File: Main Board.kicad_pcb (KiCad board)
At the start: 4 copper layers, 161 x 92 mm, 369 parts, among them J1 Motor Y, J10 CA58SUB-B, J11 PC6 EPSON MAINBOARD, J12 Y AXIS, J13 Z AXIS, J14 LED 1, J15 LED 2, J16 Power Input, J17 VS, J18 12V, J19 5V, J2 Motor Z, J20 3.3V, J21 TABLE SENSOR, J22 INPUT1, J23 INPUT2, J24 PHOTO SENSOR EMITER, J25 PHOTO SENSOR RECEIVER, J26 ANALOG, J27 INPUT3, J28 OUT1, J29 OUT2, J3 USB_B, J30 RELAY, J31 EMERGENCY, J32 EPSON POWER IN, J33 EPSON BOARD POWER, J34 Display, J35 SPI Interface, J36 I2C Interface, J37 LED4, J38 LED3, J39 Key 3, J4 SWD, J40 Key 4, J41 Key 1, J42 Key 2, J5 DEBUG, J6 LIMIT Y BACK, J7 LIMIT Y FRONT, J8 LIMIT Z UP, J9 LIMIT Z DOWN, K1 S13-24V-2C, Q1 2N7002K, Q10 2N7002K, Q11 BC817, Q12 BC817, Q13 BC817, Q14 2N7002K, Q15 2N7002K, Q16 2N7002K, Q17 BC817, Q18 2N7002K, Q19 2N7002K, Q2 2N7002K, Q20 2N7002K, Q21 2N7002K, Q3 2N7002K, Q4 2N7002K, Q5 2N7002K, Q6 2N7002K, Q7 2N7002K, Q8 YJS9435A, Q9 2N7002K, U1 TMC2209-LA, U10 74HC2G32, U11 74HC245, U12 SHTC3, U2 TMC2209-LA, U3 STM32F401VETx, U4 USBUF02W6, U5 74HC245, U6 MCP16301, U7 A4403, U8 MCP16301, U9 MCP6002-xSN, Y1 8MHz

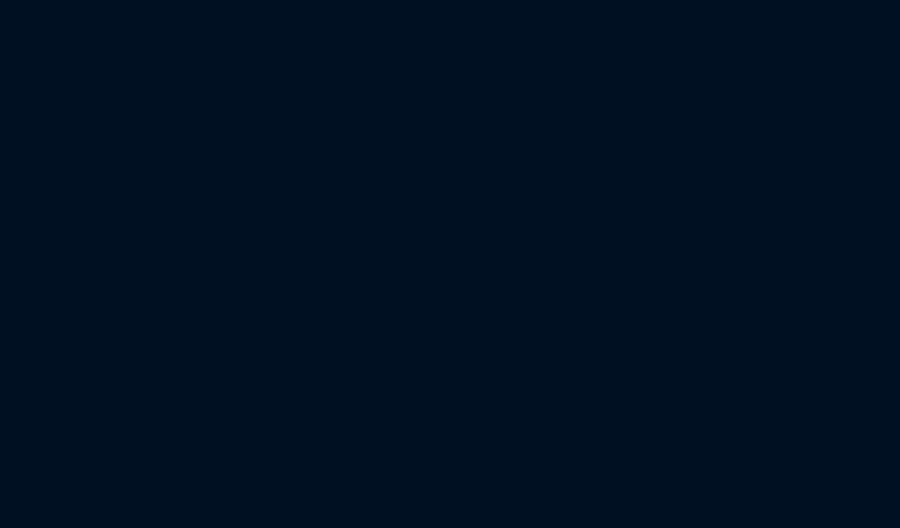
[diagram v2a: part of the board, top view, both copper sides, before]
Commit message: Added rotary encoder input
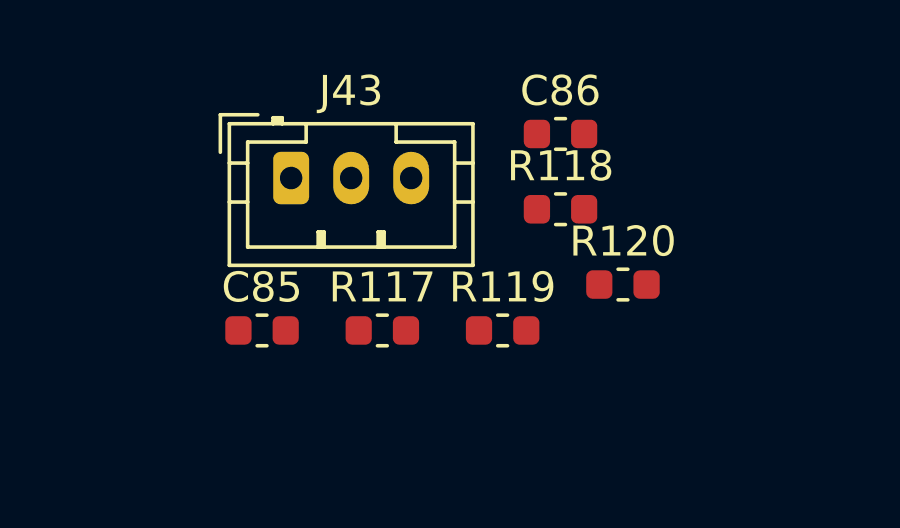
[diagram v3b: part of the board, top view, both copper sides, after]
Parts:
- added C85: 0.01uF, Capacitor_SMD:C_0603_1608Metric, F.Cu at (174.0, 8.41)
- added C86: 0.01uF, Capacitor_SMD:C_0603_1608Metric, F.Cu at (184.0, 1.86)
- added J43: Encoder, Connector_JST:JST_PH_B3B-PH-K_1x03_P2.00mm_Vertical, F.Cu at (175.0, 3.33)
- added R117: 10kΩ, Resistor_SMD:R_0603_1608Metric, F.Cu at (178.0, 8.41)
- added R118: 10kΩ, Resistor_SMD:R_0603_1608Metric, F.Cu at (184.0, 4.37)
- added R119: 10kΩ, Resistor_SMD:R_0603_1608Metric, F.Cu at (182.0, 8.41)
- added R120: 10kΩ, Resistor_SMD:R_0603_1608Metric, F.Cu at (186.0, 6.88)
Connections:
- net SWO renamed ENC2_B
- U3 pad 77: Net-(U3-Pad77) -> ENC2_A

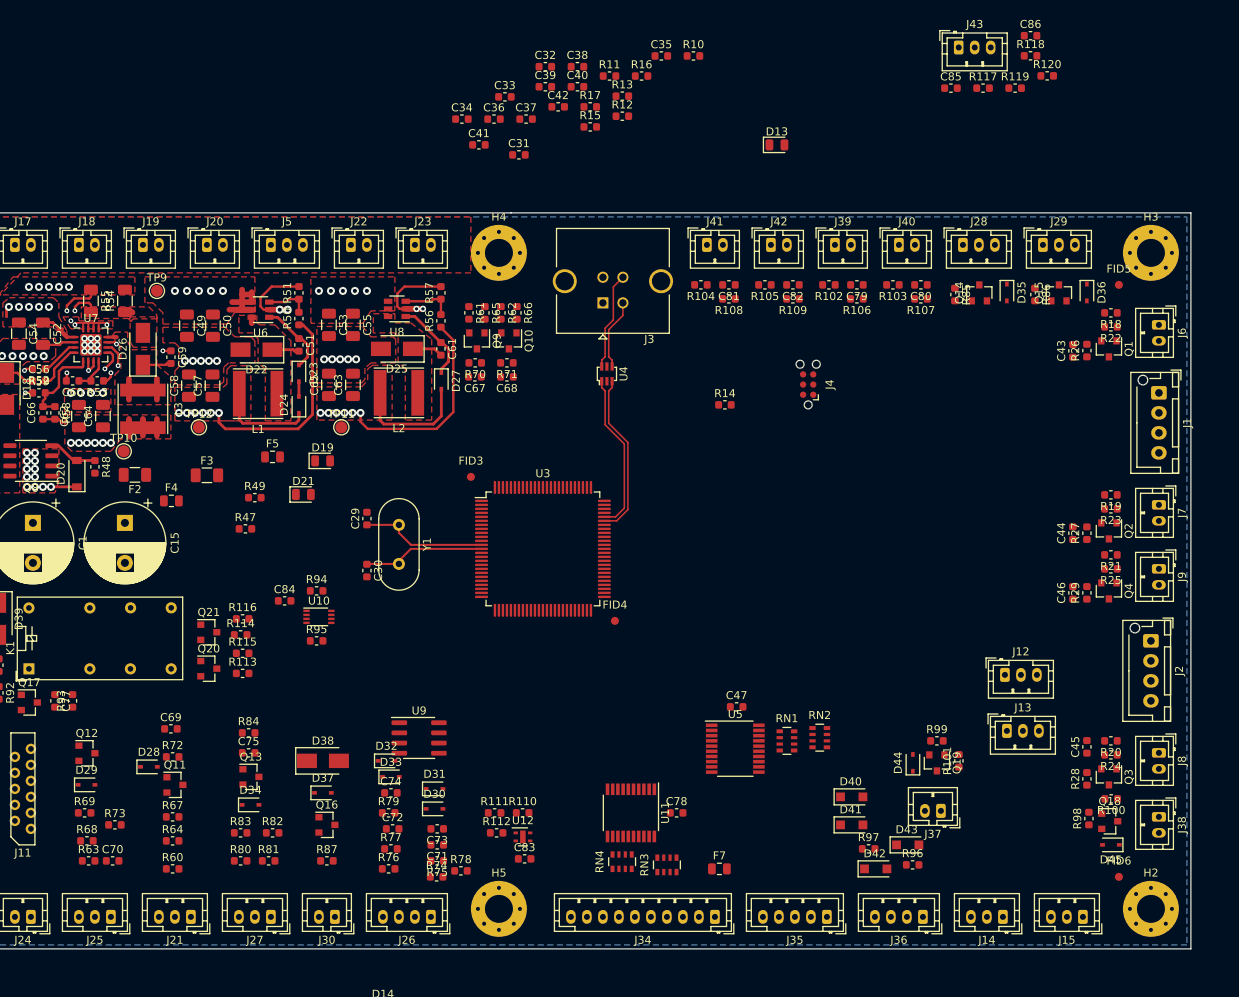
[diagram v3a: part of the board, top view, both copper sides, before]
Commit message: Modify pin attribute, routing keys input
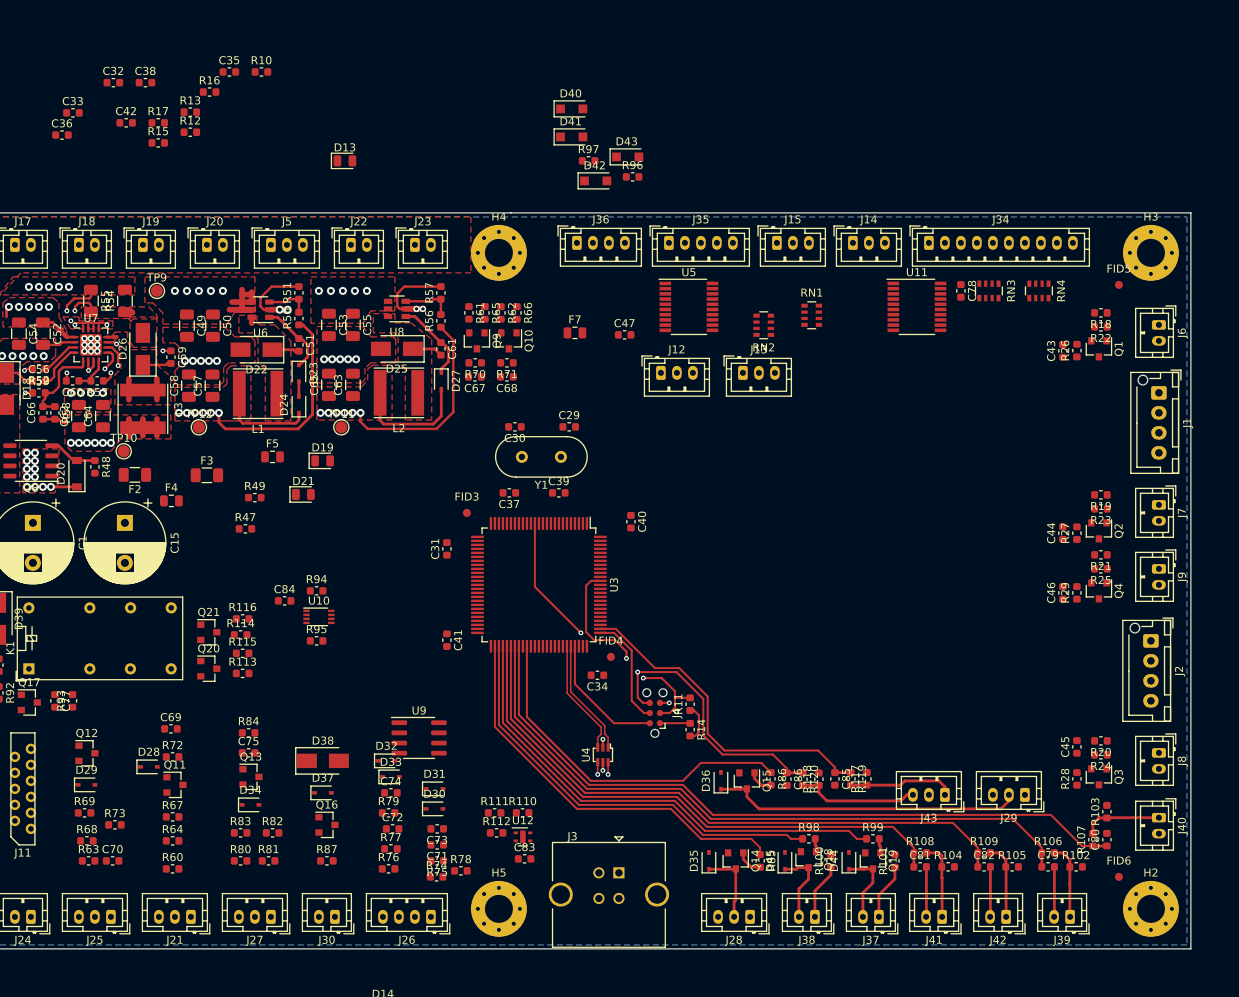
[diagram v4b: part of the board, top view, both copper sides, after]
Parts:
- moved C86 97.8 mm to (153.5, 94.8), turned to 270 degrees
- moved J36 94.7 mm to (127.2, 27.8), turned to 0 degrees
- moved R118 94.2 mm to (157.5, 94.8), turned to 90 degrees
- moved J43 93.4 mm to (173.2, 96.8), turned to 180 degrees
- moved R120 93.1 mm to (155.5, 94.8), turned to 270 degrees
- moved D40 92.8 mm to (126.6, 11.0)
- moved D41 92.8 mm to (126.6, 14.5)
- moved D42 92.8 mm to (129.6, 20.0)
- moved D43 92.8 mm to (133.6, 17.0)
- moved R96 92.8 mm to (134.2, 19.5)
- moved R97 92.8 mm to (128.7, 17.5)
- moved J15 92.5 mm to (152.2, 27.8), turned to 0 degrees
- moved J39 89.0 mm to (188.9, 112.0), turned to 180 degrees
- moved J41 89.0 mm to (172.9, 112.0), turned to 180 degrees
- moved J42 89.0 mm to (180.9, 112.0), turned to 180 degrees
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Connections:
- R30 pad 1: PE_SIGNAL -> OPE_SIGNAL
- R41 pad 1: PC1_SIGNAL -> OPC1_SIGNAL
- U3 pad 1: LIMIT_Y_FRONT -> LCD_DB6
- U3 pad 15: /Microcontroller/LED_STATUS -> Net-(U3-Pad15)
- U3 pad 16: RELAY -> INPUT2
- U3 pad 17: INPUT2 -> INPUT1
- U3 pad 18: INPUT1 -> /Microcontroller/LED_STATUS
- U3 pad 2: LIMIT_Z_UP -> LCD_DB7
- U3 pad 25: PE_SIGNAL -> 5V_DETECT
- U3 pad 26: Net-(U3-Pad26) -> 12V_DETECT
- U3 pad 29: Net-(U3-Pad29) -> EMERGENCY
- U3 pad 3: LIMIT_Z_DOWN -> LCD_E
- U3 pad 33: OUTPUT1 -> OPC1_SIGNAL
- U3 pad 34: OUTPUT2 -> OPE_SIGNAL
- U3 pad 38: LCD_RS -> PHOTO_SENSOR
- U3 pad 39: LCD_E -> TABLE_SENSOR
- U3 pad 40: LCD_DB4 -> INPUT3
- U3 pad 41: LCD_DB5 -> RELAY
- U3 pad 42: LCD_DB6 -> PRINTER_POWER_DETECT
- U3 pad 43: LCD_DB7 -> Net-(U3-Pad43)
- U3 pad 44: INPUT3 -> Net-(U3-Pad44)
- U3 pad 45: PRINTER_POWER_DETECT -> Net-(U3-Pad45)
- U3 pad 46: TABLE_SENSOR -> Net-(U3-Pad46)
- U3 pad 51: EMERGENCY -> Net-(U3-Pad51)
- U3 pad 52: Net-(U3-Pad52) -> OUTPUT1
- U3 pad 60: Net-(U3-Pad60) -> OUTPUT2
- U3 pad 61: 5V_DETECT -> Net-(U3-Pad61)
- U3 pad 62: 12V_DETECT -> Net-(U3-Pad62)
- U3 pad 7: PHOTO_SENSOR -> LCD_RS
- U3 pad 78: PC1_SIGNAL -> LIMIT_Z_UP
- U3 pad 79: Net-(U3-Pad79) -> Z_INDEX
- U3 pad 80: Net-(U3-Pad80) -> Z_DIAG
- U3 pad 81: Z_DIAG -> Z_ENABLE
- U3 pad 82: Z_INDEX -> LIMIT_Z_DOWN
- U3 pad 83: Z_ENABLE -> LIMIT_Y_FRONT
- U3 pad 84: Y_DIAG -> Y_INDEX
- U3 pad 85: Y_INDEX -> Y_DIAG
- U3 pad 95: Net-(U3-Pad95) -> LIMIT_Y_BACK
- U3 pad 97: Net-(U3-Pad97) -> LCD_DB4
- U3 pad 98: LIMIT_Y_BACK -> LCD_DB5
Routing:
- net KEY_4: track 0.00 -> 88.9 mm
- net KEY_3: track 0.00 -> 83.9 mm
- net KEY_2: track 0.00 -> 76.5 mm
- net KEY_1: track 0.00 -> 69.1 mm
- net LED4: track 0.00 -> 61.0 mm
- net LED3: track 0.00 -> 53.7 mm
- net ENC2_B: track 0.00 -> 50.9 mm, vias 0 -> 2
- net OUTPUT1: track 0.00 -> 50.3 mm
- net OUTPUT2: track 0.00 -> 44.1 mm
- net ENC2_A: track 0.00 -> 41.9 mm
- net Net-(D36-Pad1): track 0.00 -> 38.8 mm
- net NRST: track 0.00 -> 36.9 mm, vias 0 -> 2
- net GND: track 74.9 -> 95.9 mm, vias 46 -> 48
- net SWDIO: track 0.00 -> 16.1 mm
- net Net-(C29-Pad1): track 15.9 -> 0.00 mm
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
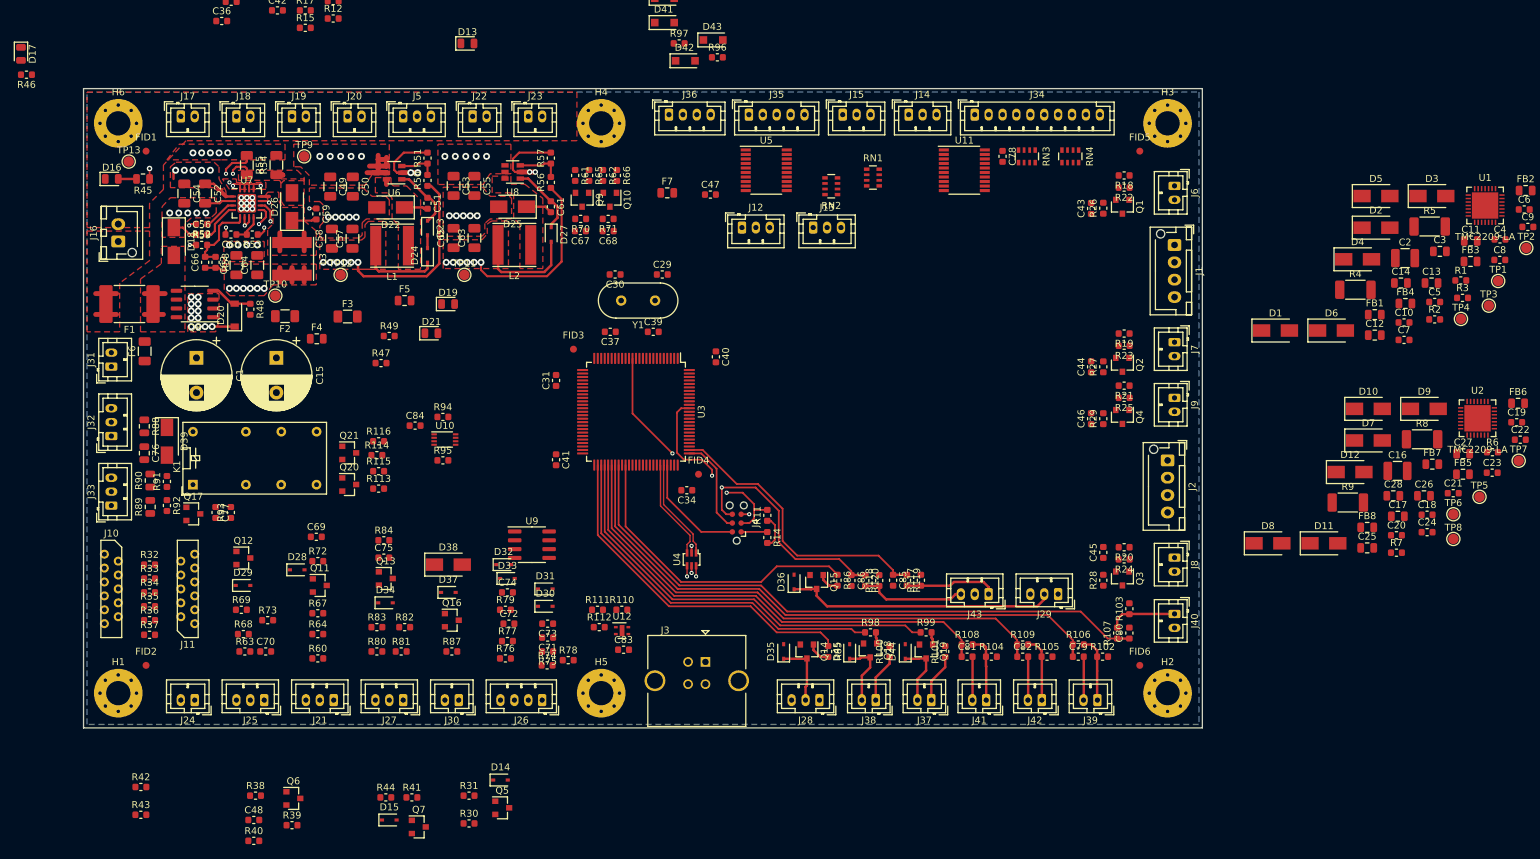
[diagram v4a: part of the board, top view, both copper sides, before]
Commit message: Routing emergnency, photo barier, relay, voltage detect, analog, footprint improvment
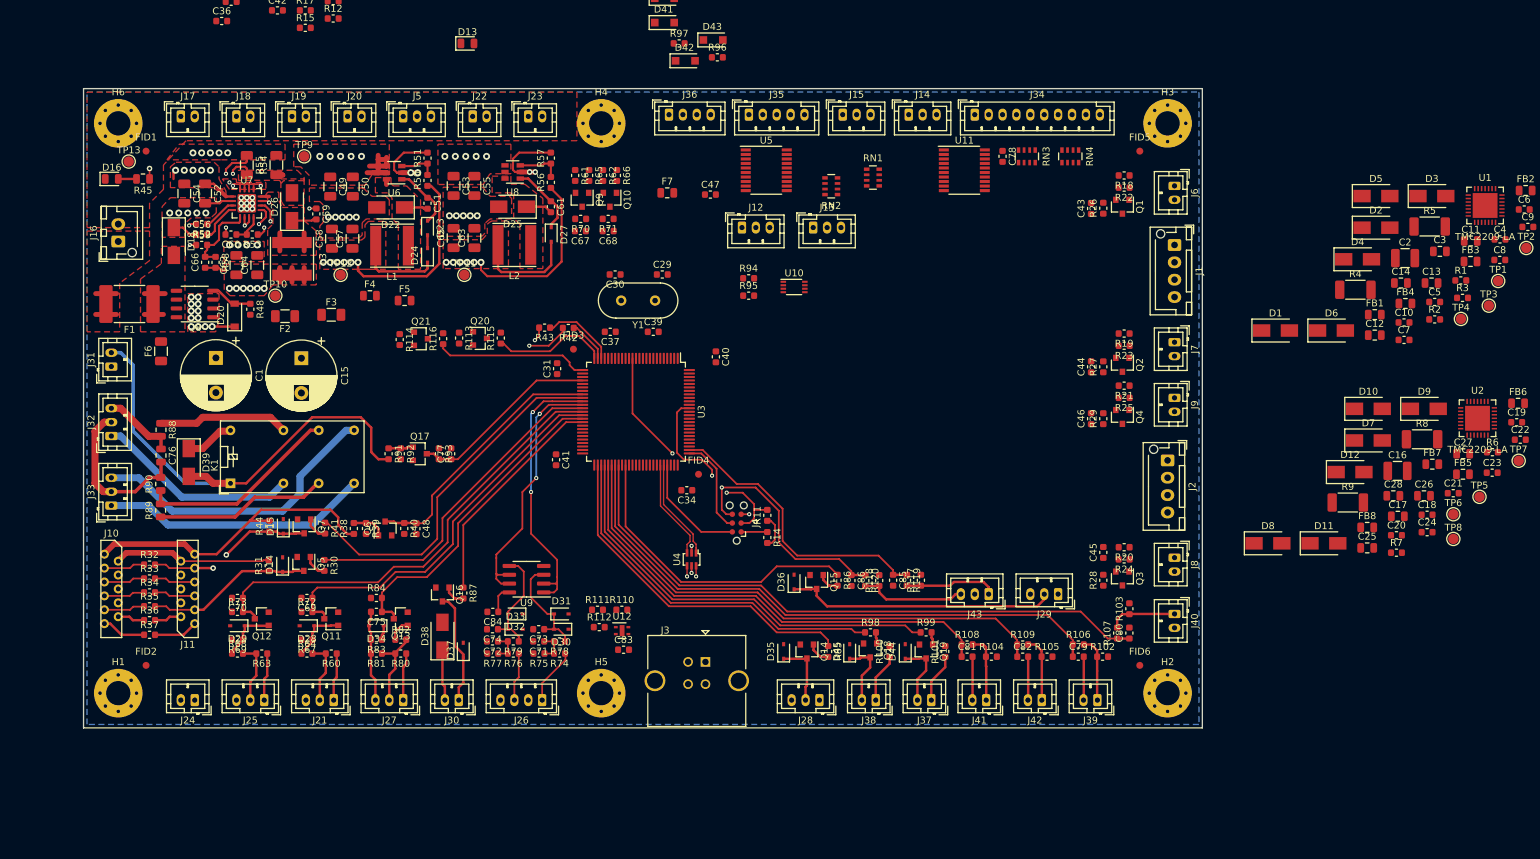
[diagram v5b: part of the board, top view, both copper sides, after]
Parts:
- removed D17, D19, D21: OF-SMD2012G-1, Diode_SMD:D_0805_2012Metric
- removed R46: 330Ω, Resistor_SMD:R_0603_1608Metric
- removed R47: 1kΩ, Resistor_SMD:R_0603_1608Metric
- removed R49: 2.7kΩ, Resistor_SMD:R_0603_1608Metric
- U1, U2: footprint footprints:TMC2209-LA -> footprints:QFN-28_5X5_3X8_EPAD
- moved R43 91.0 mm to (109.3, 58.4), turned to 180 degrees
- moved R42 90.3 mm to (112.8, 58.5), turned to 180 degrees
- moved U10 54.8 mm to (145.2, 52.5)
- moved R95 50.0 mm to (138.7, 53.8)
- moved R40 49.9 mm to (89.2, 87.3), turned to 270 degrees
- moved R94 48.3 mm to (138.7, 51.3)
- moved C48 48.0 mm to (90.9, 87.3), turned to 270 degrees
- moved Q7 46.3 mm to (74.8, 87.0), turned to 270 degrees
- moved Q5 45.2 mm to (74.7, 92.4), turned to 270 degrees
- moved D15 44.9 mm to (71.8, 87.0), turned to 90 degrees
- moved D14 44.1 mm to (71.7, 92.5), turned to 90 degrees
- moved R39 44.0 mm to (83.7, 87.3), turned to 270 degrees
- moved R31 43.9 mm to (69.7, 92.7), turned to 90 degrees
- moved R30 42.6 mm to (77.7, 92.6), turned to 270 degrees
- moved R44 42.5 mm to (69.8, 87.0), turned to 90 degrees
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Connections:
- U3 pad 33: OPC1_SIGNAL -> PRINTER_POWER_DETECT
- U3 pad 34: OPE_SIGNAL -> OPC1_SIGNAL
- U3 pad 37: Net-(U3-Pad37) -> OPE_SIGNAL
- U3 pad 42: PRINTER_POWER_DETECT -> Net-(U3-Pad42)
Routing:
- net /Sockets/PF_B: track 0.00 -> 87.3 mm, vias 0 -> 1
- net /Sockets/PF_A: track 0.00 -> 85.8 mm, vias 0 -> 1
- net Net-(D39-Pad2): track 0.00 -> 68.2 mm
- net PHOTO_SENSOR: track 0.00 -> 66.7 mm
- net TABLE_SENSOR: track 0.00 -> 56.7 mm
- net OPC1_SIGNAL: track 0.00 -> 51.8 mm
- net OPE_SIGNAL: track 0.00 -> 48.1 mm
- net INPUT3: track 0.00 -> 46.5 mm
- net /Sockets/3.3V: track 0.00 -> 44.6 mm
- net Net-(J33-Pad3): track 0.00 -> 43.2 mm
- net AIN8: track 0.00 -> 39.1 mm, vias 0 -> 2
- net Net-(J33-Pad1): track 0.00 -> 38.6 mm
- net PRINTER_POWER_DETECT: track 0.00 -> 37.8 mm
- net AIN9: track 0.00 -> 37.2 mm, vias 0 -> 2
- net RELAY: track 0.00 -> 32.3 mm
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
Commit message: Start TMC routing
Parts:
- removed TP1, TP5: Z_OB2, TestPoint:TestPoint_Pad_D1.5mm
- removed TP2, TP6: Z_OB1, TestPoint:TestPoint_Pad_D1.5mm
- removed TP3, TP7: Z_OA2, TestPoint:TestPoint_Pad_D1.5mm
- removed TP4, TP8: Z_OA1, TestPoint:TestPoint_Pad_D1.5mm
- moved U2 88.5 mm to (155.4, 78.8), turned to 270 degrees
- moved FB6 71.1 mm to (179.2, 80.3), turned to 180 degrees
- moved R8 64.6 mm to (171.2, 77.8)
- moved FB5 62.4 mm to (179.2, 78.3), turned to 180 degrees
- moved FB7 58.1 mm to (179.2, 82.3), turned to 180 degrees
- moved D9 54.7 mm to (181.4, 73.5), turned to 90 degrees
- moved R9 53.8 mm to (171.2, 84.8)
- moved FB8 48.7 mm to (179.2, 84.3), turned to 180 degrees
- moved D7 44.7 mm to (185.4, 88.5), turned to 270 degrees
- moved D10 42.6 mm to (185.4, 73.5), turned to 90 degrees
- moved D12 34.9 mm to (190.9, 85.0), turned to 90 degrees
- moved D11 33.0 mm to (190.9, 77.0), turned to 90 degrees
- moved D8 32.1 mm to (181.4, 88.5), turned to 270 degrees
- moved C45 4.05 mm to (189.7, 94.8), turned to 270 degrees
- moved R28 3.99 mm to (189.8, 90.8)
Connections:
- J3 pad 1: Net-(J3-Pad1) -> (no net)
- U1 pad 1: Net-(FB4-Pad2) -> Net-(FB1-Pad2)
- U1 pad 10: Net-(U1-Pad10) -> (no net)
- U1 pad 13: Net-(U1-Pad13) -> (no net)
- U1 pad 17: Net-(U1-Pad17) -> (no net)
- U1 pad 20: Net-(U1-Pad20) -> (no net)
- U1 pad 21: Net-(FB2-Pad2) -> Net-(FB4-Pad2)
- U1 pad 24: Net-(FB1-Pad2) -> Net-(FB3-Pad2)
- U1 pad 25: Net-(U1-Pad25) -> (no net)
- U1 pad 26: Net-(FB3-Pad2) -> Net-(FB2-Pad2)
- U1 pad 7: Net-(U1-Pad7) -> (no net)
- U12 pad 5: Net-(U12-Pad5) -> (no net)
- U2 pad 1: Net-(FB8-Pad2) -> Net-(FB5-Pad2)
- U2 pad 10: Net-(U2-Pad10) -> (no net)
- U2 pad 13: Net-(U2-Pad13) -> (no net)
- U2 pad 17: Net-(U2-Pad17) -> (no net)
- U2 pad 20: Net-(U2-Pad20) -> (no net)
- U2 pad 21: Net-(FB6-Pad2) -> Net-(FB8-Pad2)
- U2 pad 24: Net-(FB5-Pad2) -> Net-(FB7-Pad2)
- U2 pad 25: Net-(U2-Pad25) -> (no net)
- U2 pad 26: Net-(FB7-Pad2) -> Net-(FB6-Pad2)
- U2 pad 7: Net-(U2-Pad7) -> (no net)
- U2 pad 9: Net-(U2-Pad9) -> (no net)
- U3 pad 15: Net-(U3-Pad15) -> (no net)
- U3 pad 42: Net-(U3-Pad42) -> (no net)
- U3 pad 43: Net-(U3-Pad43) -> (no net)
- U3 pad 44: Net-(U3-Pad44) -> (no net)
- U3 pad 45: Net-(U3-Pad45) -> (no net)
- U3 pad 46: Net-(U3-Pad46) -> (no net)
- U3 pad 47: Net-(U3-Pad47) -> (no net)
- U3 pad 51: Net-(U3-Pad51) -> (no net)
- U3 pad 59: Net-(U3-Pad59) -> (no net)
- U3 pad 61: Net-(U3-Pad61) -> (no net)
- U3 pad 62: Net-(U3-Pad62) -> (no net)
- U3 pad 65: Net-(U3-Pad65) -> (no net)
- U3 pad 68: Net-(U3-Pad68) -> (no net)
- U3 pad 69: Net-(U3-Pad69) -> (no net)
- U3 pad 8: Net-(U3-Pad8) -> (no net)
- U3 pad 9: Net-(U3-Pad9) -> (no net)
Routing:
- net LIMIT_Z_UP: track 0.00 -> 75.7 mm
- net Net-(J8-Pad1): track 0.00 -> 8.32 mm
- net Net-(Q3-Pad1): track 0.00 -> 2.75 mm
- net Net-(FB5-Pad2): track 0.00 -> 2.30 mm
- net Net-(FB8-Pad2): track 0.00 -> 1.93 mm
- net Net-(C22-Pad1): track 0.00 -> 1.13 mm
- net Net-(C24-Pad1): track 0.00 -> 1.04 mm
- net Net-(FB7-Pad2): track 0.00 -> 0.98 mm
- net Net-(FB6-Pad2): track 0.00 -> 0.97 mm
- net GND: vias 48 -> 56
- added copper zone on F.Cu, net Net-(C22-Pad1)
- added copper zone on F.Cu, net Net-(C24-Pad1)
- added copper zone on F.Cu, net Net-(C25-Pad2)
- added copper zone on F.Cu, net Net-(C26-Pad1)
- added copper zone on F.Cu, net Net-(C27-Pad2)
- added copper zone on F.Cu, net Net-(C28-Pad1)
- added copper zone on F.Cu, net Net-(FB5-Pad2)
- added copper zone on F.Cu, net Net-(FB6-Pad2)
- added copper zone on F.Cu, net Net-(FB7-Pad2)
- added copper zone on F.Cu, net Net-(FB8-Pad2)
